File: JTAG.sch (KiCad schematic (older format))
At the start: 40 parts, among them J11 MOLEX_87831-1420, J14 Conn_ARM_JTAG_SWD_10, Q17 BSS139, Q5 BSS139, U10 NC7SZ66P5X, U7 NC7SZ66P5X, U8 SN74AVC2T245RSWR, U9 SN74AVC2T245RSWR

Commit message: DDR terminations changed, HTML BoM with variant added
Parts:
- removed C193, C358, C359: 100nF, Capacitors SMD:CAPC0603X33N, symbol AMC_FMC_Carrier-PcbDoc-rescue:C-Device
- added C193, C358, C359: CC0201_100NF_6.3V_10%_X5R, CAPC0603X33N, symbol Capacitors_SMD:CC0201_100NF_6.3V_10%_X5R

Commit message: SW2 placement changed, BOM cleared, FPGA boot, less ERC errors and wornings
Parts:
- U8, U9: footprint QFN40P140X180X55-10N -> ICs And Semiconductors SMD:QFN40P140X180X55-10N

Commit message: BOM updated, 25MHz clock level fixed
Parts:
- J11: symbol AMC_FMC_Carrier-PcbDoc-rescue:MOLEX_87831-1420-MOLEX -> AMC_FMC_Carrier-PcbDoc-rescue:MOLEX_87831-1420-MOLEX-AMC_FMC_Carrier-PcbDoc-rescue
- J14: symbol AMC_FMC_Carrier-PcbDoc-rescue:Conn_ARM_JTAG_SWD_10-Connector -> AMC_FMC_Carrier-PcbDoc-rescue:Conn_ARM_JTAG_SWD_10-Connector-AMC_FMC_Carrier-PcbDoc-rescue
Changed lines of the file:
@@
 	10050 4150 10500 4150
 $Comp
-L AMC_FMC_Carrier-PcbDoc-rescue:MOLEX_87831-1420-MOLEX J11
+L AMC_FMC_Carrier-PcbDoc-rescue:MOLEX_87831-1420-MOLEX-AMC_FMC_Carrier-PcbDoc-rescue J11
 U 1 1 5CB763C1
 P 4200 4700
@@
 MMC_TDI
 $Comp
-L AMC_FMC_Carrier-PcbDoc-rescue:Conn_ARM_JTAG_SWD_10-Connector J?
+L AMC_FMC_Carrier-PcbDoc-rescue:Conn_ARM_JTAG_SWD_10-Connector-AMC_FMC_Carrier-PcbDoc-rescue J?
 U 1 1 5E9BF6F9
 P 5500 3450

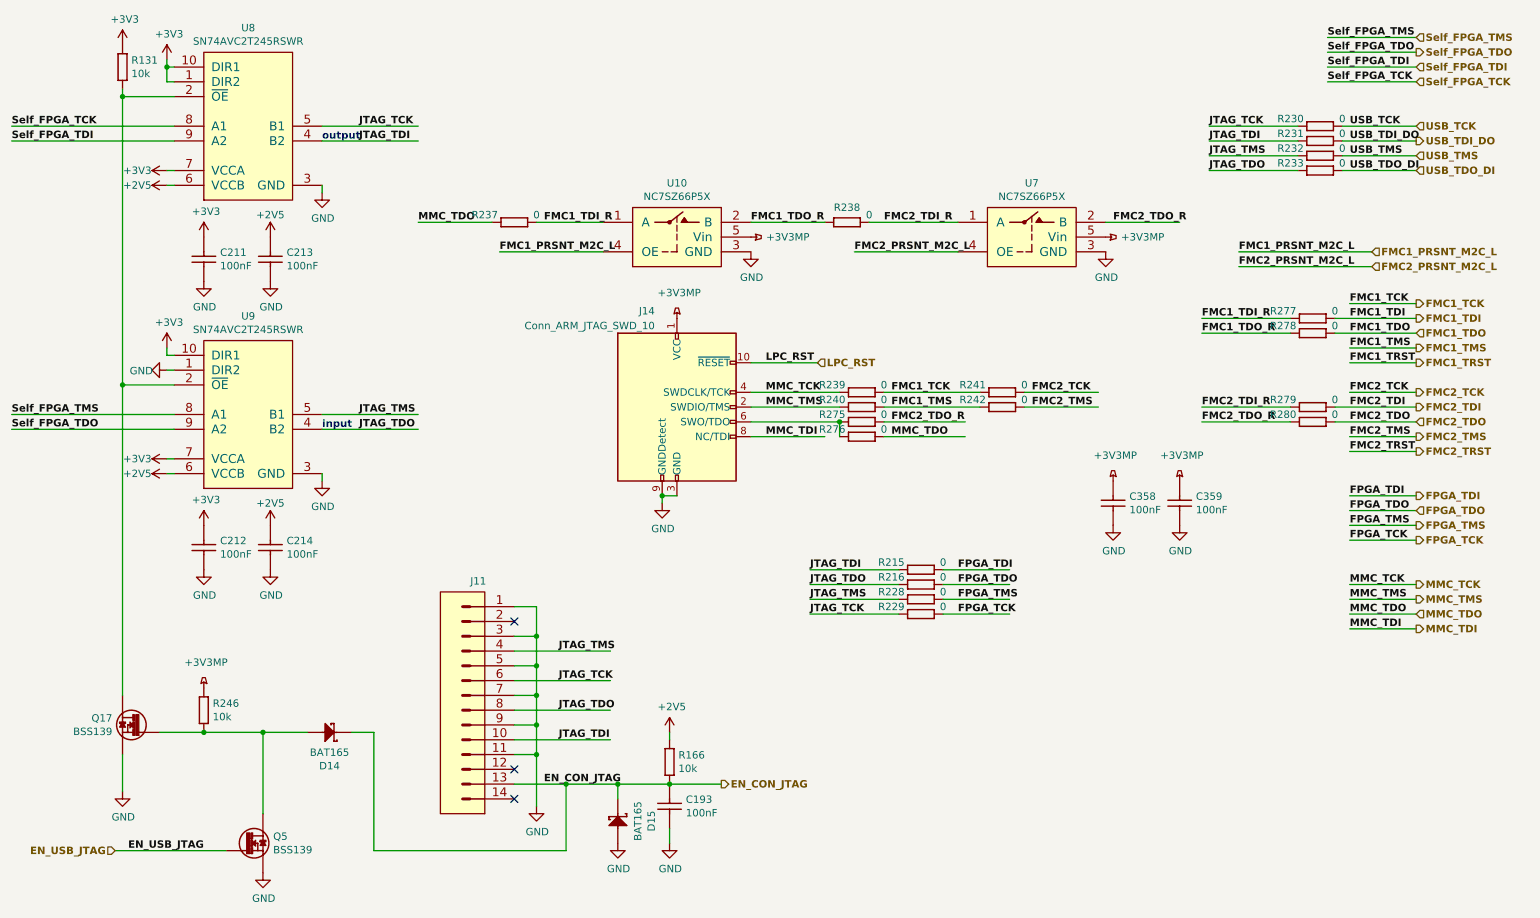
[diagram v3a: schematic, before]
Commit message: new FMC JTAG chain connected to MMC GPIO
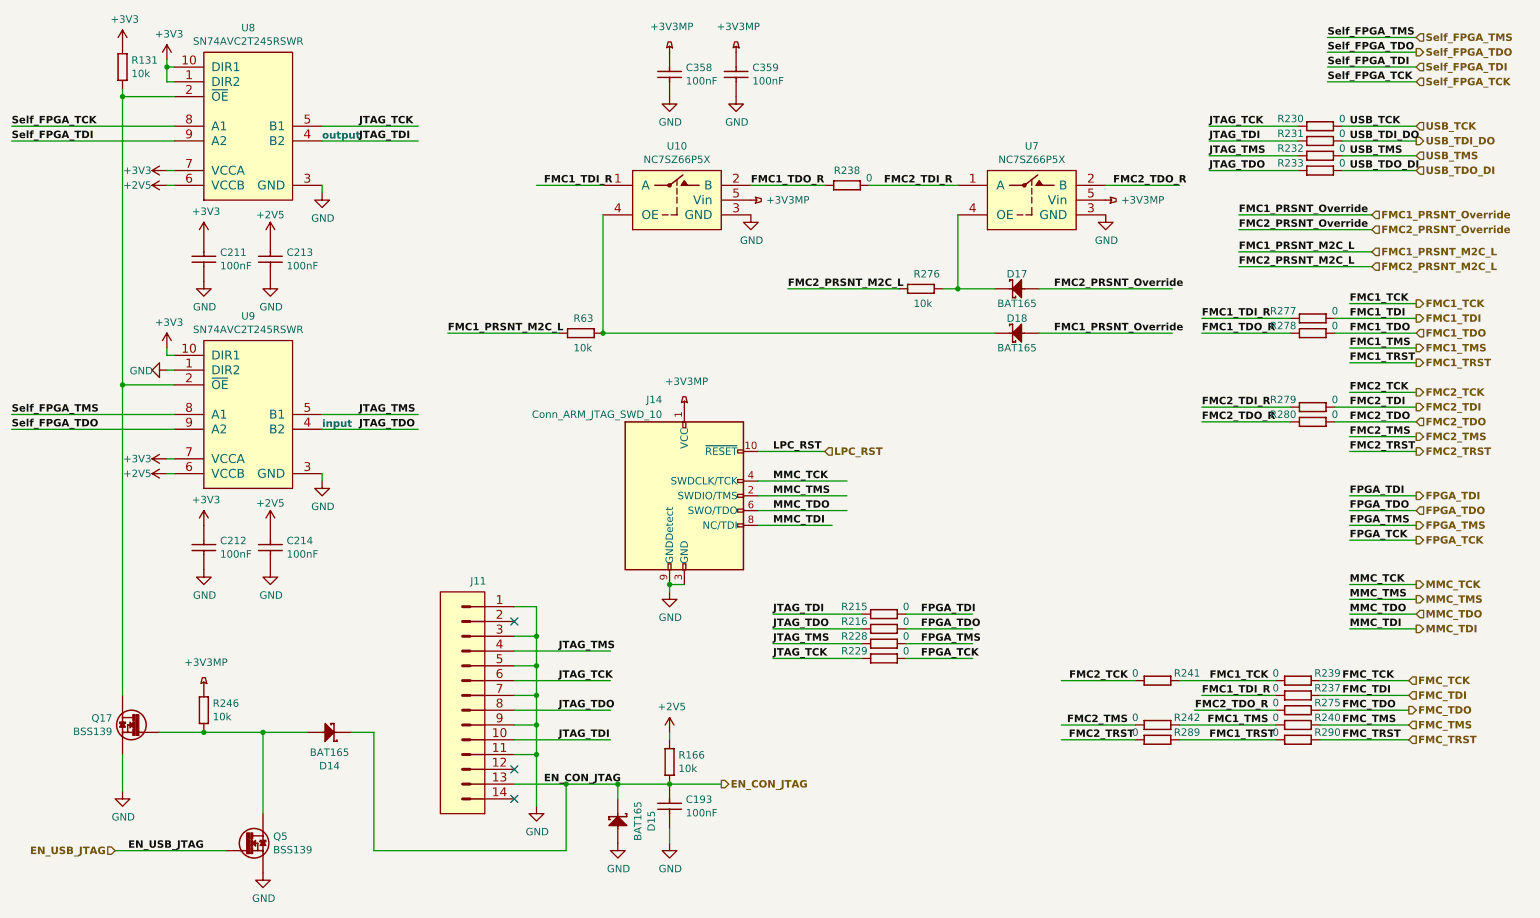
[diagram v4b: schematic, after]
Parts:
- removed R276: R0402_0R_JUMPER, RESC1005X40N, symbol Resistors_SMD:R0402_0R_JUMPER
- added D17, D18: BAT165, ICs And Semiconductors SMD:SOD2512X110N, symbol Diodes:BAT165
- added R276, R63: R0402_10K_1%_0.0625W_100PPM, RESC1005X40N, symbol Resistors_SMD:R0402_10K_1%_0.0625W_100PPM
- added R289, R290: R0402_0R_JUMPER, RESC1005X40N, symbol Resistors_SMD:R0402_0R_JUMPER
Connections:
- net labels added: FMC1_PRSNT_Override, FMC2_PRSNT_Override, FMC_TCK, FMC_TDI, FMC_TDO, FMC_TMS, FMC_TRST
- wire segments 124 -> 138
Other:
- moved on the sheet: C358, C359, J14, R215, R216, R228, R229, R237, R238, R239, R240, R241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

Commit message: BOM configuration file edited, updated Marble picture, some components part number changed
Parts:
- D14, D15, D17, D18: Manufacturer Part Number BAT165 -> BAT165AX
- J14: value Conn_ARM_JTAG_SWD_10 -> GRPB052VWQP-RC; Manufacturer Part Number (none) -> GRPB052VWQP-RC; PN WURTH_62101021021 -> (none)
- Q17, Q5: Manufacturer Part Number BSS139 -> BSS139H6327XTSA1
- U10, U7: symbol Standard_Logic:NC7SZ66P5X -> AMC_FMC_Carrier-PcbDoc-rescue:NC7SZ66P5X-Standard_Logic
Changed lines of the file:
@@
 EN_CON_JTAG
 $Comp
-L Standard_Logic:NC7SZ66P5X U7
+L AMC_FMC_Carrier-PcbDoc-rescue:NC7SZ66P5X-Standard_Logic U7
 U 1 1 5E17EE5A
 P 7600 1850
@@
 $EndComp
 $Comp
-L Standard_Logic:NC7SZ66P5X U10
+L AMC_FMC_Carrier-PcbDoc-rescue:NC7SZ66P5X-Standard_Logic U10
 U 1 1 5E17F12A
 P 5200 1850
@@
 AR Path="/5CA40231/5E9BF6F9" Ref="J14"  Part="1"
 F 0 "J14" H 5400 4700 50  0000 R CNN
-F 1 "Conn_ARM_JTAG_SWD_10" H 5400 4600 50  0000 R CNN
+F 1 "GRPB052VWQP-RC" H 5400 4600 50  0000 R CNN
 F 2 "Connector_PinHeader_1.27mm:PinHeader_2x05_P1.27mm_Vertical_SMD" H 5600 3500 50  0001 L TNN
 F 3 "http://infocenter.arm.com/help/topic/com.arm.doc.faqs/attached/13634/cortex_debug_connectors.pdf" V 5200 2800 50  0001 C CNN
-F 4 "WURTH_62101021021" H 5550 4050 50  0001 C CNN "PN"
+F 4 "GRPB052VWQP-RC" H 5550 4050 50  0001 C CNN "Manufacturer Part Number"
 	1    5550 4050
 	1    0    0    -1
@@
 F 13 "250V 30mA N-Channel  SIPMOS® Small-Signal-Transistor" H 2000 4170 60  0001 L CNN "Part Description"
 F 14 "INFINEON" H 2000 4080 60  0001 L CNN "Manufacturer"
-F 15 "BSS139" H 2000 3990 60  0001 L CNN "Manufacturer Part Number"
+F 15 "BSS139H6327XTSA1" H 2000 3990 60  0001 L CNN "Manufacturer Part Number"
 F 16 "3" H 2000 3900 60  0001 L CNN "Pin Count"
 F 17 "SOT23-3" H 2000 3810 60  0001 L CNN "Case"
@@
 F 15 "Medium Power AF Schottky Diode" H 5100 4810 60  0001 L CNN "Part Description"
 F 16 "INFINEON" H 5100 4720 60  0001 L CNN "Manufacturer"
-F 17 "BAT165" H 5100 4630 60  0001 L CNN "Manufacturer Part Number"
+F 17 "BAT165AX" H 5100 4630 60  0001 L CNN "Manufacturer Part Number"
 F 18 "2" H 5100 4540 60  0001 L CNN "Pin Count"
 F 19 "SOD323" H 5100 4450 60  0001 L CNN "Case"
@@
 F 15 "Medium Power AF Schottky Diode" H 3000 4060 60  0001 L CNN "Part Description"
 F 16 "INFINEON" H 3000 3970 60  0001 L CNN "Manufacturer"
-F 17 "BAT165" H 3000 3880 60  0001 L CNN "Manufacturer Part Number"
+F 17 "BAT165AX" H 3000 3880 60  0001 L CNN "Manufacturer Part Number"
 F 18 "2" H 3000 3790 60  0001 L CNN "Pin Count"
 F 19 "SOD323" H 3000 3700 60  0001 L CNN "Case"
@@
 F 13 "250V 30mA N-Channel  SIPMOS® Small-Signal-Transistor" H 2450 4970 60  0001 L CNN "Part Description"
 F 14 "INFINEON" H 2450 4880 60  0001 L CNN "Manufacturer"
-F 15 "BSS139" H 2450 4790 60  0001 L CNN "Manufacturer Part Number"
+F 15 "BSS139H6327XTSA1" H 2450 4790 60  0001 L CNN "Manufacturer Part Number"
 F 16 "3" H 2450 4700 60  0001 L CNN "Pin Count"
 F 17 "SOT23-3" H 2450 4610 60  0001 L CNN "Case"
@@
 F 15 "Medium Power AF Schottky Diode" H 7950 1060 60  0001 L CNN "Part Description"
 F 16 "INFINEON" H 7950 970 60  0001 L CNN "Manufacturer"
-F 17 "BAT165" H 7950 880 60  0001 L CNN "Manufacturer Part Number"
+F 17 "BAT165AX" H 7950 880 60  0001 L CNN "Manufacturer Part Number"
 F 18 "2" H 7950 790 60  0001 L CNN "Pin Count"
 F 19 "SOD323" H 7950 700 60  0001 L CNN "Case"
@@
 F 15 "Medium Power AF Schottky Diode" H 7950 1360 60  0001 L CNN "Part Description"
 F 16 "INFINEON" H 7950 1270 60  0001 L CNN "Manufacturer"
-F 17 "BAT165" H 7950 1180 60  0001 L CNN "Manufacturer Part Number"
+F 17 "BAT165AX" H 7950 1180 60  0001 L CNN "Manufacturer Part Number"
 F 18 "2" H 7950 1090 60  0001 L CNN "Pin Count"
 F 19 "SOD323" H 7950 1000 60  0001 L CNN "Case"

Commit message: applied all required amendments to the project
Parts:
- Q17, Q5: value BSS139 -> BSS138LT1G; footprint SOT95P240X110-3N -> ICs And Semiconductors SMD:SOT95P240X110-3N; symbol Transistors:BSS139 -> Transistors:BSS138LT1G; Comment =Device -> BSS138LT1G; ComponentHeight 1.1mm -> 1.11mm; ComponentLink1Description ~~ -> (none); ComponentLink2Description ~~ -> (none); CreateDate 09/23/14 00:00:00 -> 03/23/09 00:00:00; Database Table Name (none) -> Transistors; Device BSS139 -> BSS138LT1G; Footprint Library (none) -> ICs And Semiconductors SMD; LatestRevisionDate 09/23/14 00:00:00 -> 03/23/09 00:00:00; Library Name ICs And Semiconductors SMD -> ICs And Semiconductors.DbLib; Manufacturer INFINEON -> ON SEMICONDUCTOR; Manufacturer Part Number BSS139H6327XTSA1 -> BSS138LT1G; Part Description 250V 30mA N-Channel SIPMOS® Small-Signal-Transistor -> 50V 200mA N-Channel Enhancement Mode Field-Effect Transistor; Part Number BSS139 -> BSS138LT1G; SCEM (none) -> (none); Sense Comment ~~ -> (none); Status ~~ -> (none); Status Comment ~~ -> (none)
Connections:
- wire segments 138 -> 139
- no-connect marks 3 -> 2

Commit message: Rename library AMC_FMC_Carrier-PcbDoc-rescue as marble_misc
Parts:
- J11: symbol AMC_FMC_Carrier-PcbDoc-rescue:MOLEX_87831-1420-MOLEX-AMC_FMC_Carrier-PcbDoc-rescue -> marble_misc:MOLEX_87831-1420-MOLEX-AMC_FMC_Carrier-PcbDoc-rescue
- J14: symbol AMC_FMC_Carrier-PcbDoc-rescue:Conn_ARM_JTAG_SWD_10-Connector-AMC_FMC_Carrier-PcbDoc-rescue -> marble_misc:Conn_ARM_JTAG_SWD_10-Connector-AMC_FMC_Carrier-PcbDoc-rescue
- U10, U7: symbol AMC_FMC_Carrier-PcbDoc-rescue:NC7SZ66P5X-Standard_Logic -> marble_misc:NC7SZ66P5X-Standard_Logic
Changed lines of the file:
@@
 	10050 4150 10500 4150
 $Comp
-L AMC_FMC_Carrier-PcbDoc-rescue:MOLEX_87831-1420-MOLEX-AMC_FMC_Carrier-PcbDoc-rescue J11
+L marble_misc:MOLEX_87831-1420-MOLEX-AMC_FMC_Carrier-PcbDoc-rescue J11
 U 1 1 5CB763C1
 P 4200 4700
@@
 EN_CON_JTAG
 $Comp
-L AMC_FMC_Carrier-PcbDoc-rescue:NC7SZ66P5X-Standard_Logic U7
+L marble_misc:NC7SZ66P5X-Standard_Logic U7
 U 1 1 5E17EE5A
 P 7600 1850
@@
 $EndComp
 $Comp
-L AMC_FMC_Carrier-PcbDoc-rescue:NC7SZ66P5X-Standard_Logic U10
+L marble_misc:NC7SZ66P5X-Standard_Logic U10
 U 1 1 5E17F12A
 P 5200 1850
@@
 MMC_TDI
 $Comp
-L AMC_FMC_Carrier-PcbDoc-rescue:Conn_ARM_JTAG_SWD_10-Connector-AMC_FMC_Carrier-PcbDoc-rescue J?
+L marble_misc:Conn_ARM_JTAG_SWD_10-Connector-AMC_FMC_Carrier-PcbDoc-rescue J?
 U 1 1 5E9BF6F9
 P 5550 4050
